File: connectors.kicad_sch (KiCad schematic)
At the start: 4 parts

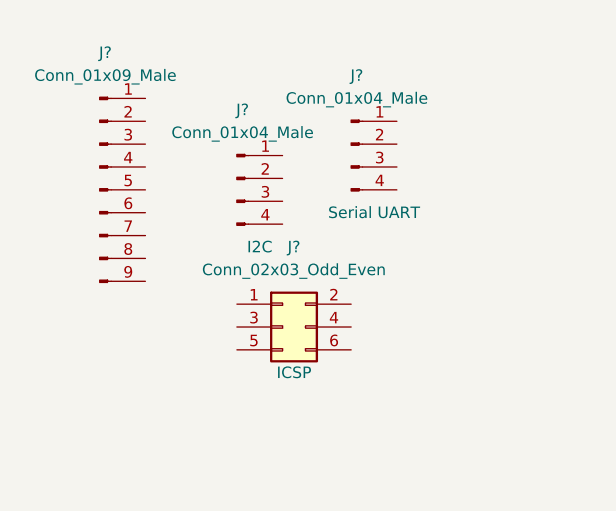
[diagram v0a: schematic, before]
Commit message: Arranged and annotated the symbols
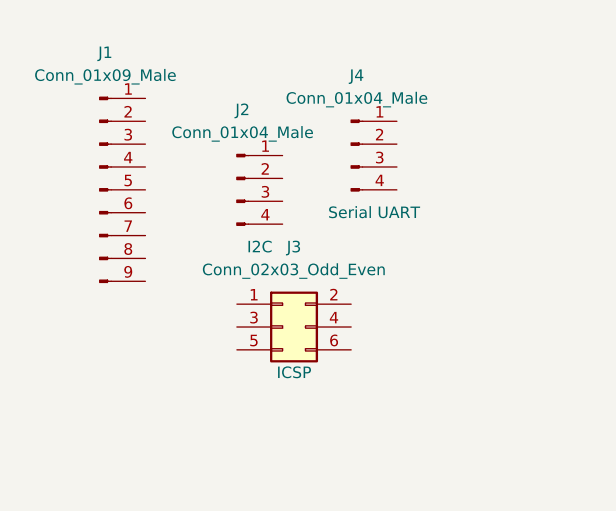
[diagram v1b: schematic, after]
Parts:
- gave numbers to parts that had none: 4
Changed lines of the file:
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@@
   (symbol (lib_id "Connector_Generic:Conn_02x03_Odd_Even") (at 60.96 60.96 0) (unit 1)
     (in_bom yes) (on_board yes)
-    (property "Reference" "J?" (id 0) (at 62.23 52.07 0))
+    (property "Reference" "J3" (id 0) (at 62.23 52.07 0))
     (property "Value" "Conn_02x03_Odd_Even" (id 1) (at 62.23 54.61 0))
     (property "Footprint" "" (id 2) (at 60.96 60.96 0)
@@
   (symbol (lib_id "Connector:Conn_01x04_Male") (at 55.88 44.45 0) (unit 1)
     (in_bom yes) (on_board yes)
-    (property "Reference" "J?" (id 0) (at 56.515 36.83 0))
+    (property "Reference" "J2" (id 0) (at 56.515 36.83 0))
     (property "Value" "Conn_01x04_Male" (id 1) (at 56.515 39.37 0))
     (property "Footprint" "" (id 2) (at 55.88 44.45 0)
@@
   (symbol (lib_id "Connector:Conn_01x09_Male") (at 40.64 45.72 0) (unit 1)
     (in_bom yes) (on_board yes) (fields_autoplaced)
-    (property "Reference" "J?" (id 0) (at 41.275 30.48 0))
+    (property "Reference" "J1" (id 0) (at 41.275 30.48 0))
     (property "Value" "Conn_01x09_Male" (id 1) (at 41.275 33.02 0))
     (property "Footprint" "" (id 2) (at 40.64 45.72 0)
@@
   (symbol (lib_id "Connector:Conn_01x04_Male") (at 68.58 40.64 0) (unit 1)
     (in_bom yes) (on_board yes)
-    (property "Reference" "J?" (id 0) (at 69.215 33.02 0))
+    (property "Reference" "J4" (id 0) (at 69.215 33.02 0))
     (property "Value" "Conn_01x04_Male" (id 1) (at 69.215 35.56 0))
     (property "Footprint" "" (id 2) (at 68.58 40.64 0)

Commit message: Import footprints. Associated the symbols to the footprints I want to use
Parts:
- J1: footprint (none) -> Connector_PinHeader_2.54mm:PinHeader_1x09_P2.54mm_Vertical
- J2, J4: footprint (none) -> Connector_PinHeader_2.54mm:PinHeader_1x04_P2.54mm_Vertical
- J3: footprint (none) -> Connector_PinHeader_2.54mm:PinHeader_2x03_P2.54mm_Vertical
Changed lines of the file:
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@@
     (property "Reference" "J3" (id 0) (at 62.23 52.07 0))
     (property "Value" "Conn_02x03_Odd_Even" (id 1) (at 62.23 54.61 0))
-    (property "Footprint" "" (id 2) (at 60.96 60.96 0)
+    (property "Footprint" "Connector_PinHeader_2.54mm:PinHeader_2x03_P2.54mm_Vertical" (id 2) (at 60.96 60.96 0)
       (effects (font (size 1.27 1.27)) hide)
     )
@@
     (property "Reference" "J2" (id 0) (at 56.515 36.83 0))
     (property "Value" "Conn_01x04_Male" (id 1) (at 56.515 39.37 0))
-    (property "Footprint" "" (id 2) (at 55.88 44.45 0)
+    (property "Footprint" "Connector_PinHeader_2.54mm:PinHeader_1x04_P2.54mm_Vertical" (id 2) (at 55.88 44.45 0)
       (effects (font (size 1.27 1.27)) hide)
     )
@@
     (property "Reference" "J1" (id 0) (at 41.275 30.48 0))
     (property "Value" "Conn_01x09_Male" (id 1) (at 41.275 33.02 0))
-    (property "Footprint" "" (id 2) (at 40.64 45.72 0)
+    (property "Footprint" "Connector_PinHeader_2.54mm:PinHeader_1x09_P2.54mm_Vertical" (id 2) (at 40.64 45.72 0)
       (effects (font (size 1.27 1.27)) hide)
     )
@@
     (property "Reference" "J4" (id 0) (at 69.215 33.02 0))
     (property "Value" "Conn_01x04_Male" (id 1) (at 69.215 35.56 0))
-    (property "Footprint" "" (id 2) (at 68.58 40.64 0)
+    (property "Footprint" "Connector_PinHeader_2.54mm:PinHeader_1x04_P2.54mm_Vertical" (id 2) (at 68.58 40.64 0)
       (effects (font (size 1.27 1.27)) hide)
     )

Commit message: finished wiring everything up.
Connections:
- net MISO: now reaches J3.1 (Pin_1)
- net Vcc: now reaches J3.2 (Pin_2)
- net Vcc: now also J1.9 (Pin_9), J2.2 (Pin_2), J4.2 (Pin_2)
- net SCK: now reaches J3.3 (Pin_3)
- net SCK: now also J2.4 (Pin_4)
- net MOSI: now reaches J3.4 (Pin_4)
- net RESET: now reaches J3.5 (Pin_5)
- net GND: now reaches J3.6 (Pin_6)
- net GND: now also J1.8 (Pin_8), J2.1 (Pin_1), J4.1 (Pin_1)
- net SDA: now reaches J2.3 (Pin_3)
- net D2: now reaches J1.1 (Pin_1)
- net D3: now reaches J1.2 (Pin_2)
- net D4: now reaches J1.3 (Pin_3)
- net D5: now reaches J1.4 (Pin_4)
- net D6: now reaches J1.5 (Pin_5)
- net D7: now reaches J1.6 (Pin_6)
- net D8: now reaches J1.7 (Pin_7)
- net RX: now reaches J4.3 (Pin_3)
- net TX: now reaches J4.4 (Pin_4)
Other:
- moved on the sheet: J1, J2, J3, J4
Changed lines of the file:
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@@
 (kicad_sch (version 20211123) (generator eeschema)
   (paper "A4")
-  (symbol (lib_id "Connector_Generic:Conn_02x03_Odd_Even") (at 60.96 60.96 0) (unit 1)
+  (hierarchical_label "SCK" (shape passive) (at 57.785 40.64 0)
+    (effects (font (size 1.27 1.27)) (justify left))
+  )
+  (hierarchical_label "D8" (shape bidirectional) (at 58.42 73.025 0)
+    (effects (font (size 1.27 1.27)) (justify left))
+  )
+  (hierarchical_label "Vcc" (shape passive) (at 88.265 62.865 0)
+    (effects (font (size 1.27 1.27)) (justify left))
+  )
+  (hierarchical_label "D5" (shape bidirectional) (at 58.42 65.405 0)
+    (effects (font (size 1.27 1.27)) (justify left))
+  )
+  (hierarchical_label "SDA" (shape bidirectional) (at 57.785 38.1 0)
+    (effects (font (size 1.27 1.27)) (justify left))
+  )
+  (hierarchical_label "Vcc" (shape passive) (at 83.185 35.56 0)
+    (effects (font (size 1.27 1.27)) (justify left))
+  )
+  (hierarchical_label "D6" (shape bidirectional) (at 58.42 67.945 0)
+    (effects (font (size 1.27 1.27)) (justify left))
+  )
+  (hierarchical_label "D2" (shape bidirectional) (at 58.42 57.785 0)
+    (effects (font (size 1.27 1.27)) (justify left))
+  )
+  (hierarchical_label "D7" (shape bidirectional) (at 58.42 70.485 0)
+    (effects (font (size 1.27 1.27)) (justify left))
+  )
+  (hierarchical_label "TX" (shape output) (at 83.185 40.64 0)
+    (effects (font (size 1.27 1.27)) (justify left))
+  )
+  (hierarchical_label "GND" (shape passive) (at 58.42 75.565 0)
+    (effects (font (size 1.27 1.27)) (justify left))
+  )
+  (hierarchical_label "RX" (shape input) (at 83.185 38.1 0)
+    (effects (font (size 1.27 1.27)) (justify left))
+  )
+  (hierarchical_label "D3" (shape bidirectional) (at 58.42 60.325 0)
+    (effects (font (size 1.27 1.27)) (justify left))
+  )
+  (hierarchical_label "MOSI" (shape input) (at 88.265 65.405 0)
+    (effects (font (size 1.27 1.27)) (justify left))
+  )
+  (hierarchical_label "RESET" (shape passive) (at 75.565 67.945 180)
+    (effects (font (size 1.27 1.27)) (justify right))
+  )
+  (hierarchical_label "GND" (shape passive) (at 88.265 67.945 0)
+    (effects (font (size 1.27 1.27)) (justify left))
+  )
+  (hierarchical_label "Vcc" (shape passive) (at 58.42 78.105 0)
+    (effects (font (size 1.27 1.27)) (justify left))
+  )
+  (hierarchical_label "MISO" (shape output) (at 75.565 62.865 180)
+    (effects (font (size 1.27 1.27)) (justify right))
+  )
+  (hierarchical_label "GND" (shape passive) (at 83.185 33.02 0)
+    (effects (font (size 1.27 1.27)) (justify left))
+  )
+  (hierarchical_label "SCK" (shape passive) (at 75.565 65.405 180)
+    (effects (font (size 1.27 1.27)) (justify right))
+  )
+  (hierarchical_label "D4" (shape bidirectional) (at 58.42 62.865 0)
+    (effects (font (size 1.27 1.27)) (justify left))
+  )
+  (hierarchical_label "Vcc" (shape passive) (at 57.785 35.56 0)
+    (effects (font (size 1.27 1.27)) (justify left))
+  )
+  (hierarchical_label "GND" (shape passive) (at 57.785 33.02 0)
+    (effects (font (size 1.27 1.27)) (justify left))
+  )
+  (symbol (lib_id "Connector_Generic:Conn_02x03_Odd_Even") (at 80.645 65.405 0) (unit 1)
     (in_bom yes) (on_board yes)
-    (property "Reference" "J3" (id 0) (at 62.23 52.07 0))
-    (property "Value" "Conn_02x03_Odd_Even" (id 1) (at 62.23 54.61 0))
-    (property "Footprint" "Connector_PinHeader_2.54mm:PinHeader_2x03_P2.54mm_Vertical" (id 2) (at 60.96 60.96 0)
+    (property "Reference" "J3" (id 0) (at 81.915 56.515 0))
+    (property "Value" "Conn_02x03_Odd_Even" (id 1) (at 81.915 59.055 0))
+    (property "Footprint" "Connector_PinHeader_2.54mm:PinHeader_2x03_P2.54mm_Vertical" (id 2) (at 80.645 65.405 0)
       (effects (font (size 1.27 1.27)) hide)
     )
-    (property "Datasheet" "~" (id 3) (at 60.96 60.96 0)
+    (property "Datasheet" "~" (id 3) (at 80.645 65.405 0)
       (effects (font (size 1.27 1.27)) hide)
     )
-    (property "Purpose" "ICSP" (id 4) (at 62.23 66.04 0))
+    (property "Purpose" "ICSP" (id 4) (at 81.915 70.485 0))
     (pin "1")
     (pin "2")
@@
     (pin "6")
   )
-  (symbol (lib_id "Connector:Conn_01x04_Male") (at 55.88 44.45 0) (unit 1)
+  (symbol (lib_id "Connector:Conn_01x04_Male") (at 52.705 35.56 0) (unit 1)
     (in_bom yes) (on_board yes)
-    (property "Reference" "J2" (id 0) (at 56.515 36.83 0))
-    (property "Value" "Conn_01x04_Male" (id 1) (at 56.515 39.37 0))
-    (property "Footprint" "Connector_PinHeader_2.54mm:PinHeader_1x04_P2.54mm_Vertical" (id 2) (at 55.88 44.45 0)
+    (property "Reference" "J2" (id 0) (at 53.34 27.94 0))
+    (property "Value" "Conn_01x04_Male" (id 1) (at 53.34 30.48 0))
+    (property "Footprint" "Connector_PinHeader_2.54mm:PinHeader_1x04_P2.54mm_Vertical" (id 2) (at 52.705 35.56 0)
       (effects (font (size 1.27 1.27)) hide)
     )
-    (property "Datasheet" "~" (id 3) (at 55.88 44.45 0)
+    (property "Datasheet" "~" (id 3) (at 52.705 35.56 0)
       (effects (font (size 1.27 1.27)) hide)
     )
-    (property "Purpose" "I2C" (id 4) (at 58.42 52.07 0))
+    (property "Purpose" "I2C" (id 4) (at 55.245 43.18 0))
     (pin "1")
     (pin "2")
@@
     (pin "4")
   )
-  (symbol (lib_id "Connector:Conn_01x09_Male") (at 40.64 45.72 0) (unit 1)
+  (symbol (lib_id "Connector:Conn_01x09_Male") (at 53.34 67.945 0) (unit 1)
     (in_bom yes) (on_board yes) (fields_autoplaced)
-    (property "Reference" "J1" (id 0) (at 41.275 30.48 0))
-    (property "Value" "Conn_01x09_Male" (id 1) (at 41.275 33.02 0))
-    (property "Footprint" "Connector_PinHeader_2.54mm:PinHeader_1x09_P2.54mm_Vertical" (id 2) (at 40.64 45.72 0)
+    (property "Reference" "J1" (id 0) (at 53.975 52.705 0))
+    (property "Value" "Conn_01x09_Male" (id 1) (at 53.975 55.245 0))
+    (property "Footprint" "Connector_PinHeader_2.54mm:PinHeader_1x09_P2.54mm_Vertical" (id 2) (at 53.34 67.945 0)
       (effects (font (size 1.27 1.27)) hide)
     )
-    (property "Datasheet" "~" (id 3) (at 40.64 45.72 0)
+    (property "Datasheet" "~" (id 3) (at 53.34 67.945 0)
       (effects (font (size 1.27 1.27)) hide)
     )
@@
     (pin "9")
   )
-  (symbol (lib_id "Connector:Conn_01x04_Male") (at 68.58 40.64 0) (unit 1)
+  (symbol (lib_id "Connector:Conn_01x04_Male") (at 78.105 35.56 0) (unit 1)
     (in_bom yes) (on_board yes)
-    (property "Reference" "J4" (id 0) (at 69.215 33.02 0))
-    (property "Value" "Conn_01x04_Male" (id 1) (at 69.215 35.56 0))
-    (property "Footprint" "Connector_PinHeader_2.54mm:PinHeader_1x04_P2.54mm_Vertical" (id 2) (at 68.58 40.64 0)
+    (property "Reference" "J4" (id 0) (at 78.74 27.94 0))
+    (property "Value" "Conn_01x04_Male" (id 1) (at 78.74 30.48 0))
+    (property "Footprint" "Connector_PinHeader_2.54mm:PinHeader_1x04_P2.54mm_Vertical" (id 2) (at 78.105 35.56 0)
       (effects (font (size 1.27 1.27)) hide)
     )
-    (property "Datasheet" "~" (id 3) (at 68.58 40.64 0)
+    (property "Datasheet" "~" (id 3) (at 78.105 35.56 0)
       (effects (font (size 1.27 1.27)) hide)
     )
-    (property "Purpose" "Serial UART" (id 4) (at 71.12 48.26 0))
+    (property "Purpose" "Serial UART" (id 4) (at 80.645 43.18 0))
     (pin "1")
     (pin "2")

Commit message: Fix schematic defect. SCK changed to SCL
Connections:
- net SCK: no longer J2.4 (Pin_4)
- new net SCL: J2.4 (Pin_4)
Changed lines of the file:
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@@
 (kicad_sch (version 20211123) (generator eeschema)
   (paper "A4")
-  (hierarchical_label "SCK" (shape passive) (at 57.785 40.64 0)
+  (hierarchical_label "SCL" (shape passive) (at 57.785 40.64 0)
     (effects (font (size 1.27 1.27)) (justify left))
   )
